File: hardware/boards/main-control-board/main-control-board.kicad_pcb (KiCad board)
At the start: 2 copper layers, 80.5 x 50 mm, 31 parts, among them J1 Conn_01x02_Pin_Speaker, J2 Conn_OLED, J3 Conn_extension, J7 Conn_ESP32_L, J8 Conn_ESP32_R, U1 PCA9685PW,118, U2 HX PZ2.54-3X5P ZZ, U3 MAX98357AETE+T

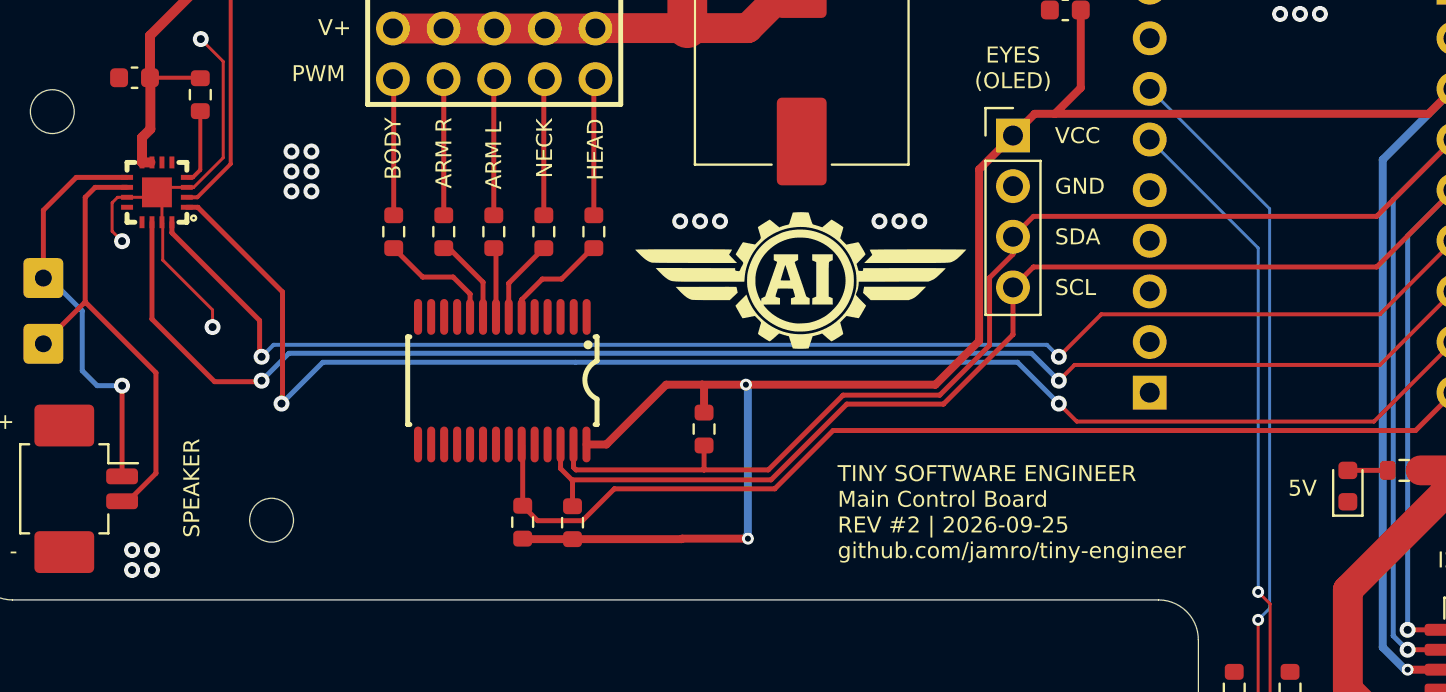
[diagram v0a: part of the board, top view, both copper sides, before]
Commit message: use basic components over extended
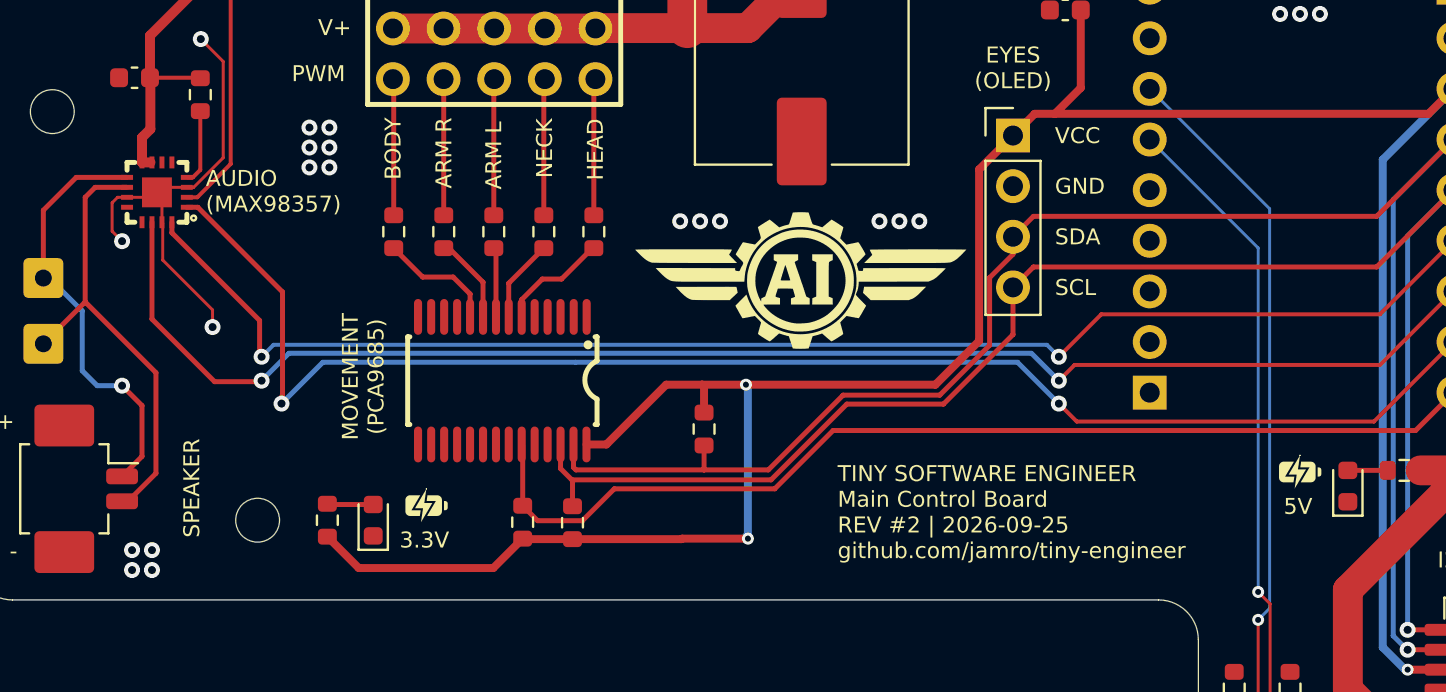
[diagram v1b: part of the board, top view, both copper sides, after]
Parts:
- added D2: LED, LED_SMD:LED_0603_1608Metric, F.Cu at (142.1, 116.0)
- added R13: 1k, Resistor_SMD:R_0603_1608Metric, F.Cu at (139.8, 116.0)
- moved H2 0.70 mm to (136.3, 116.0)
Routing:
- net +3.3V: track 115.9 -> 126.9 mm
- net Net-(D2-A): track 0.00 -> 2.02 mm
- net Net-(J1-Pin_1): track 20.8 -> 21.6 mm
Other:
- board text added: "3.3V"
- board text added: "AUDIO (MAX98357)"
- board text added: "MOVEMENT (PCA9685)"

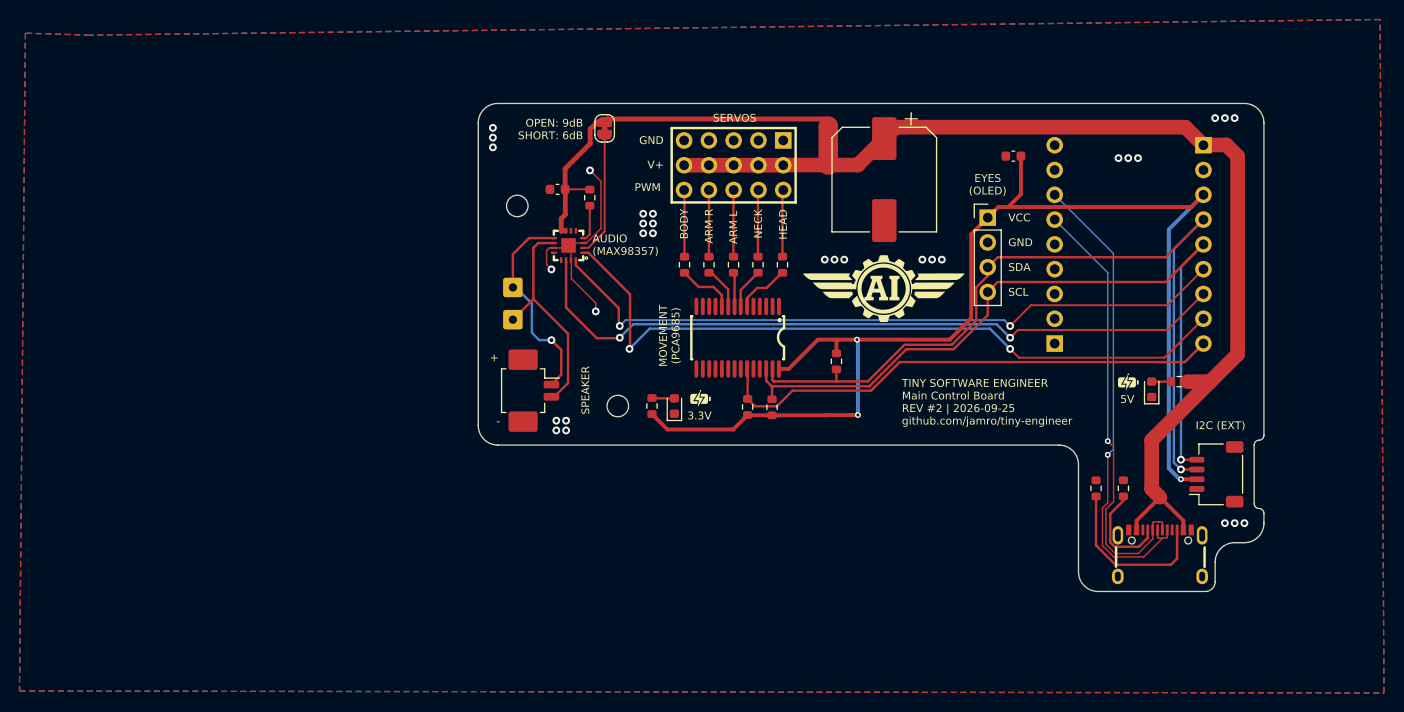
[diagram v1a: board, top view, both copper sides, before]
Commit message: add polyfuse protection
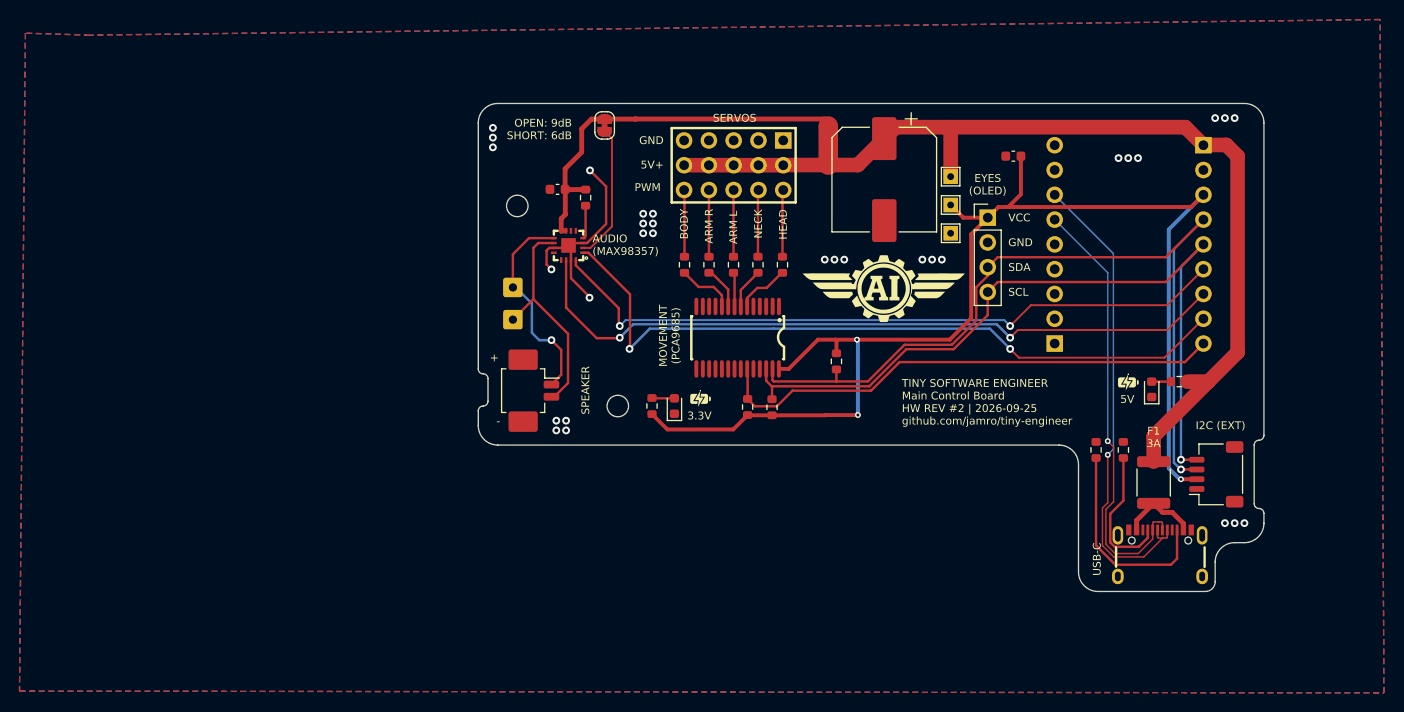
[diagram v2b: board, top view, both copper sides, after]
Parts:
- added F1: 3A PPTC, Fuse:Fuse_1812_4532Metric, F.Cu at (191.2, 123.8)
- added TP3: TestPointGND, TestPoint:TestPoint_THTPad_1.5x1.5mm_Drill0.7mm, F.Cu at (170.4, 98.3)
- added TP4: TestPoint5V, TestPoint:TestPoint_THTPad_1.5x1.5mm_Drill0.7mm, F.Cu at (170.4, 92.5)
- added TP5: TestPoint3.3V, TestPoint:TestPoint_THTPad_1.5x1.5mm_Drill0.7mm, F.Cu at (170.4, 95.4)
- moved R1 3.94 mm to (188.1, 120.5)
- moved R2 3.94 mm to (185.3, 120.5)
- moved R12 0.43 mm to (133.0, 94.7)
- moved JP1 0.30 mm to (134.9, 87.2)
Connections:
- USB1 pad A4B9: +5V -> /USB/USB_VBUS
- USB1 pad B4A9: +5V -> /USB/USB_VBUS
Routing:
- net /USB/USB_VBUS: track 0.00 -> 8.01 mm
- net +5V: track 109.6 -> 101.7 mm
- net +3.3V: track 126.9 -> 131.3 mm
- net Net-(USB1-CC2): track 17.3 -> 21.3 mm
- net Net-(USB1-CC1): track 10.5 -> 14.4 mm
- net GND: track 23.0 -> 21.8 mm
- net Net-(JP1-B): track 12.8 -> 13.9 mm
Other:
- outline, holes or cut-outs redrawn
- board text added: "+3.3V"
- board text added: "+5V"
- board text added: "5V+"
- board text added: "F1 3A"
- board text added: "TEST POINTS"
- board text added: "TINY SOFTWARE ENGINEER Main Control Board HW REV #2 | 2026-09-25 github.com/jamro/tiny-engineer"
- board text added: "USB-C"
- board text added: "USE JST OR PADS ONLY, NOT BOTH"
- board text removed: "TINY SOFTWARE ENGINEER Main Control Board REV #2 | 2026-09-25 github.com/jamro/tiny-engineer"
- board text removed: "V+"

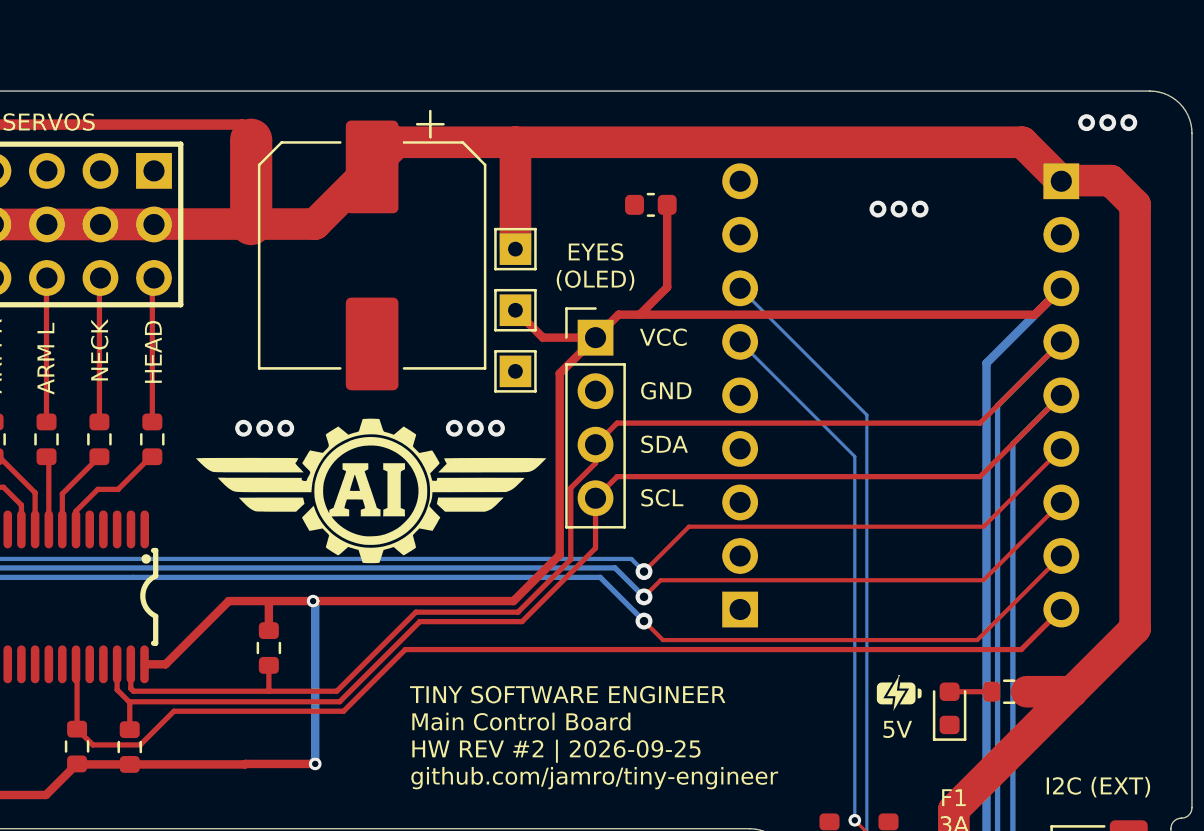
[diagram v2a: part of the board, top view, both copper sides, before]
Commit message: turn test points into extension points
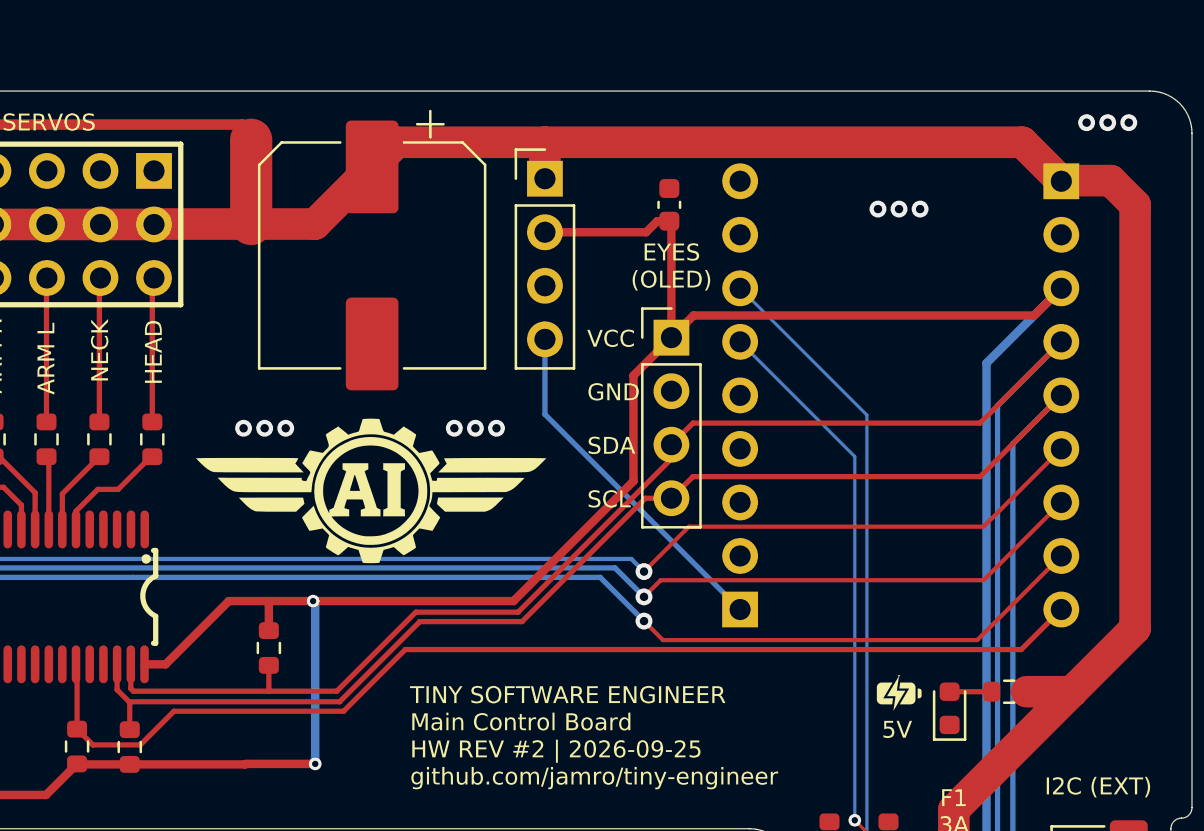
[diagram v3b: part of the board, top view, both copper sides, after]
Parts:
- removed TP3: TestPointGND, TestPoint:TestPoint_THTPad_1.5x1.5mm_Drill0.7mm
- removed TP4: TestPoint5V, TestPoint:TestPoint_THTPad_1.5x1.5mm_Drill0.7mm
- removed TP5: TestPoint3.3V, TestPoint:TestPoint_THTPad_1.5x1.5mm_Drill0.7mm
- added J4: Conn_extension_2, Connector_PinHeader_2.54mm:PinHeader_1x04_P2.54mm_Vertical, F.Cu at (171.8, 89.2)
- moved J2 3.60 mm to (177.8, 96.7)
- moved C1 0.88 mm to (177.7, 90.4), turned to -90 degrees
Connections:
- J8 pad 1: Net-(J8-Pin_1) -> /ESP32/GP6
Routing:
- net /ESP32/GP6: track 0.00 -> 16.7 mm
- net +5V: track 101.7 -> 98.4 mm
- net /I2C_SDA: track 84.7 -> 82.6 mm
- net /I2C_SCL: track 79.6 -> 78.2 mm
- net +3.3V: track 131.3 -> 130.1 mm
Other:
- board text added: "EXTENSIONS"
- board text removed: "TEST POINTS"

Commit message: pre-fab improvements
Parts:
- moved TP2 3.54 mm to (124.4, 103.8)
- moved TP1 3.43 mm to (124.5, 107.1)
- moved J1 0.70 mm to (126.4, 114.4)
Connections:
- U3 pad 10: Net-(J1-Pin_2) -> Net-(J1-Pin_1)
- U3 pad 9: Net-(J1-Pin_1) -> Net-(J1-Pin_2)
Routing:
- net GND: track 21.8 -> 24.5 mm, vias 31 -> 33
- net Net-(J1-Pin_2): track 22.9 -> 24.4 mm, vias 0 -> 1
- net /I2S_BCLK: track 71.6 -> 72.5 mm
- net Net-(USB1-CC2): track 21.3 -> 22.0 mm
- net Net-(J1-Pin_1): track 21.6 -> 21.1 mm, vias 1 -> 0

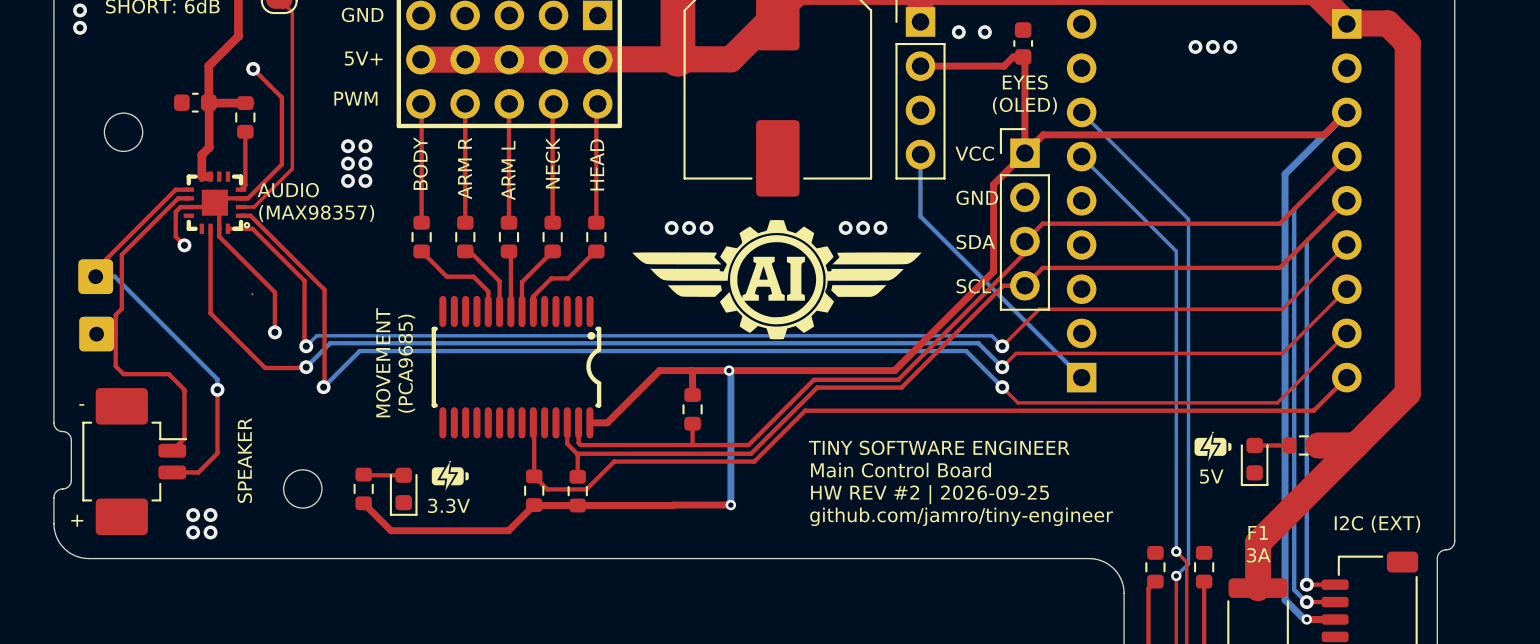
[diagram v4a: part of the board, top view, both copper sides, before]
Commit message: fix expected nets
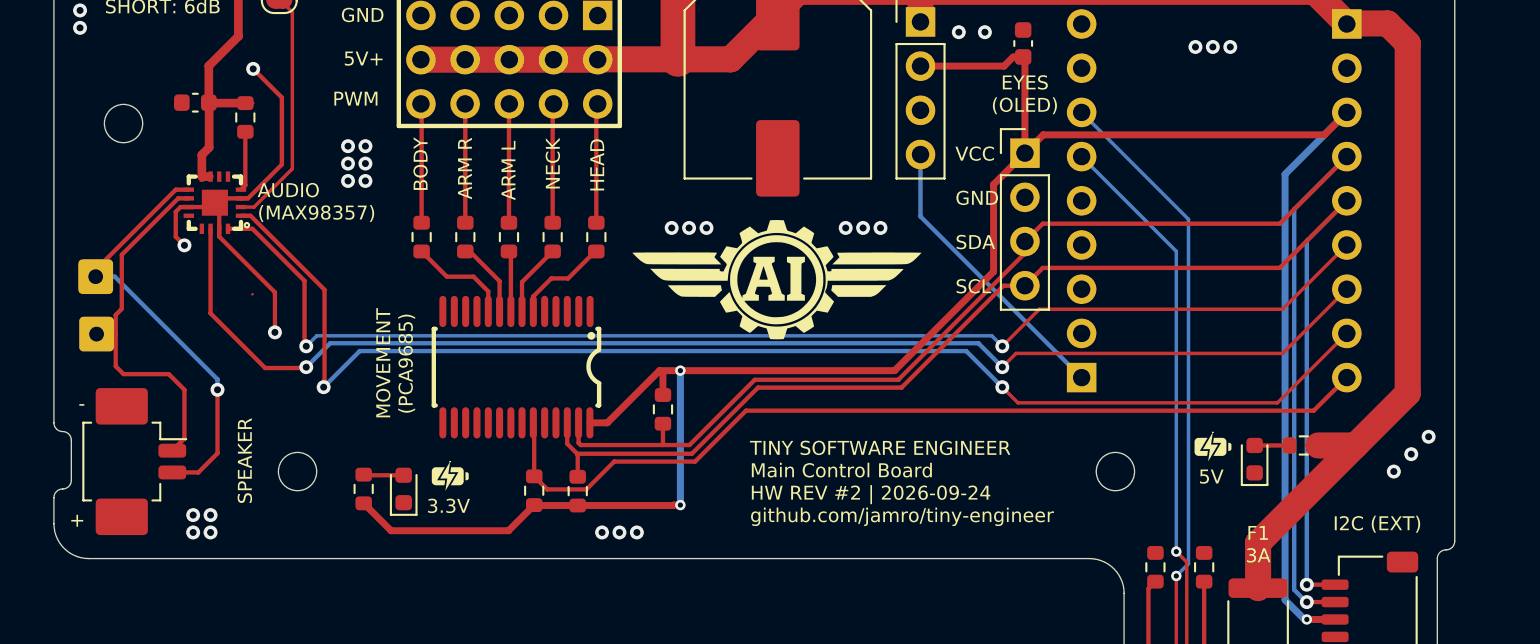
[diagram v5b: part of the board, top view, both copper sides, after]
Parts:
- added H3: MountingHole, MountingHole:MountingHole_2.2mm_M2, F.Cu at (183.0, 115.0)
- moved R5 1.70 mm to (157.0, 111.4)
- moved H2 1.04 mm to (136.0, 115.0)
- moved H1 0.50 mm to (126.0, 95.0)
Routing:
- net +3.3V: track 130.1 -> 126.8 mm
- net GND: vias 33 -> 39
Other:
- board text added: "TINY SOFTWARE ENGINEER Main Control Board HW REV #2 | 2026-09-24 github.com/jamro/tiny-engineer"
- board text removed: "TINY SOFTWARE ENGINEER Main Control Board HW REV #2 | 2026-09-25 github.com/jamro/tiny-engineer"
